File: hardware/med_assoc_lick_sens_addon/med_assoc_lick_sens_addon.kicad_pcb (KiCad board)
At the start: 2 copper layers, 50.8 x 52.1 mm, 15 parts, among them J1 Conn_Coaxial, J2 Conn_01x03_Socket, U1 6N139, U2 L7805

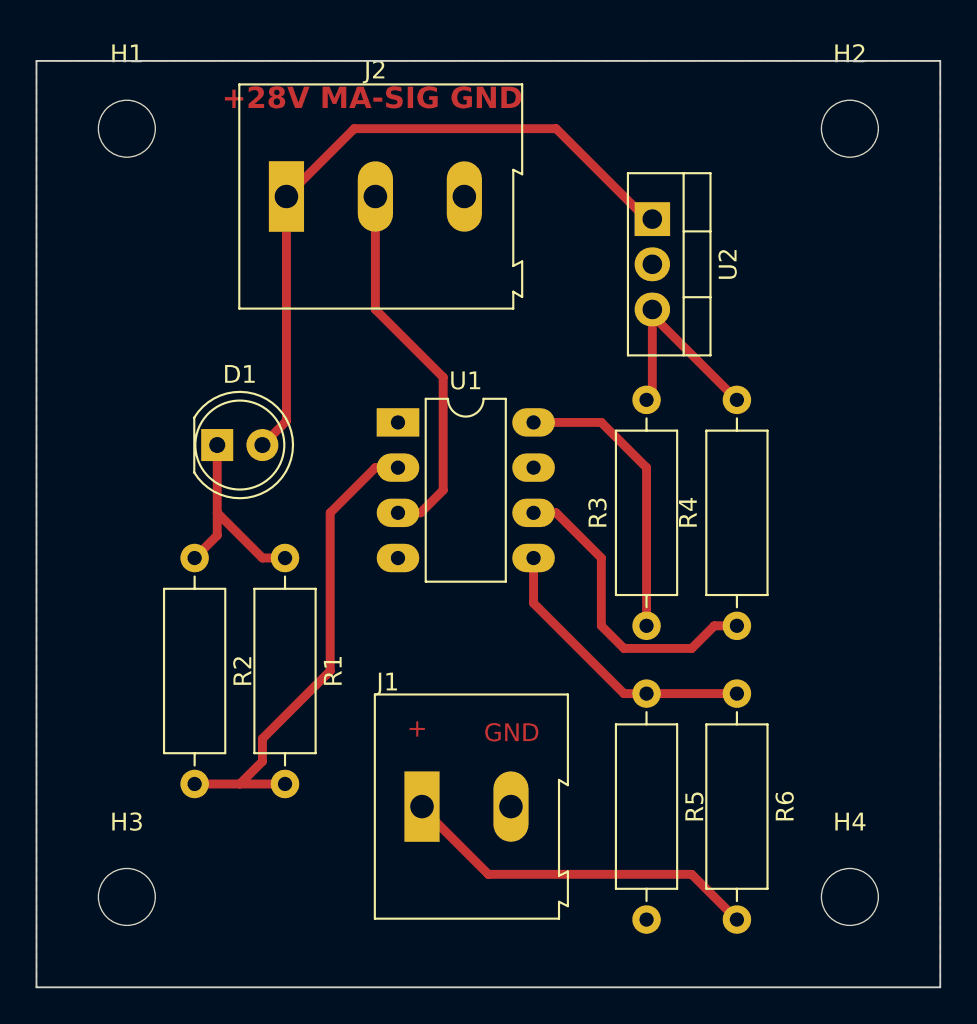
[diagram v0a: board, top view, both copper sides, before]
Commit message: move traces to bottom side of board
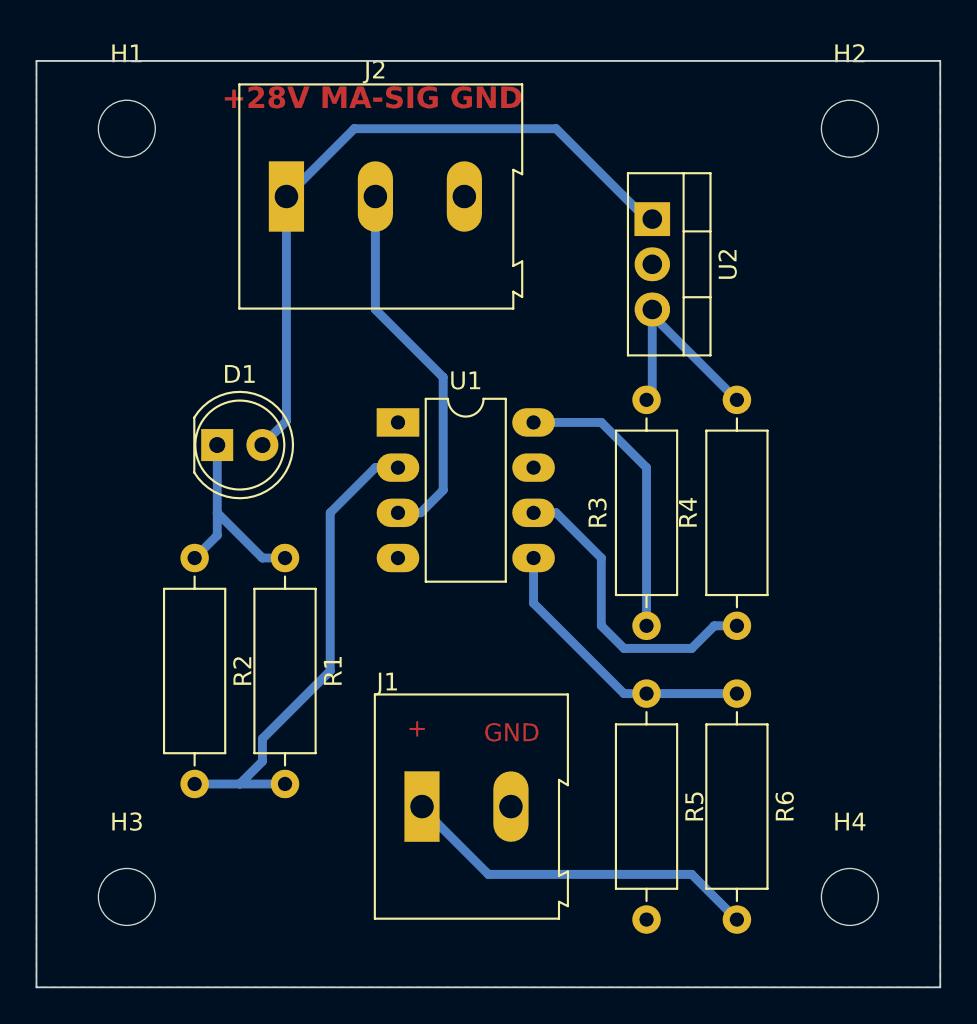
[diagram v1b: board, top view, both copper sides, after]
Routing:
- added copper zone on B.Cu, net GND
- removed copper zone on F.Cu, net GND
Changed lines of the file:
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@@
     (effects (font (size 1 1) (thickness 0.15)) (justify left bottom))
   )
-  (segment (start 152.4 63.5) (end 153.67 63.5) (width 0.5) (layer "F.Cu") (net 1))
-  (segment (start 149.86 60.96) (end 149.86 62.23) (width 0.5) (layer "F.Cu") (net 1))
-  (segment (start 149.86 57.15) (end 149.86 60.96) (width 0.5) (layer "F.Cu") (net 1))
-  (segment (start 149.86 60.96) (end 152.4 63.5) (width 0.5) (layer "F.Cu") (net 1))
-  (segment (start 149.86 62.23) (end 148.59 63.5) (width 0.5) (layer "F.Cu") (net 1))
-  (segment (start 174.315 44.45) (end 173.99 44.45) (width 0.5) (layer "F.Cu") (net 2))
-  (segment (start 153.75 43.18) (end 153.75 55.8) (width 0.5) (layer "F.Cu") (net 2))
-  (segment (start 153.75 55.8) (end 152.4 57.15) (width 0.5) (layer "F.Cu") (net 2))
-  (segment (start 168.91 39.37) (end 157.56 39.37) (width 0.5) (layer "F.Cu") (net 2))
-  (segment (start 157.56 39.37) (end 153.75 43.18) (width 0.5) (layer "F.Cu") (net 2))
-  (segment (start 173.99 44.45) (end 168.91 39.37) (width 0.5) (layer "F.Cu") (net 2))
-  (segment (start 165.1 81.28) (end 161.37 77.55) (width 0.5) (layer "F.Cu") (net 3))
-  (segment (start 161.37 77.55) (end 161.37 77.47) (width 0.5) (layer "F.Cu") (net 3))
-  (segment (start 176.53 81.28) (end 165.1 81.28) (width 0.5) (layer "F.Cu") (net 3))
-  (segment (start 179.07 83.82) (end 176.53 81.28) (width 0.5) (layer "F.Cu") (net 3))
-  (segment (start 158.75 43.18) (end 158.75 49.53) (width 0.5) (layer "F.Cu") (net 5))
-  (segment (start 162.56 59.69) (end 161.29 60.96) (width 0.5) (layer "F.Cu") (net 5))
-  (segment (start 161.29 60.96) (end 160.02 60.96) (width 0.5) (layer "F.Cu") (net 5))
-  (segment (start 158.75 49.53) (end 162.56 53.34) (width 0.5) (layer "F.Cu") (net 5))
-  (segment (start 162.56 53.34) (end 162.56 59.69) (width 0.5) (layer "F.Cu") (net 5))
-  (segment (start 151.13 76.2) (end 152.4 74.93) (width 0.5) (layer "F.Cu") (net 6))
-  (segment (start 156.21 69.85) (end 156.21 60.96) (width 0.5) (layer "F.Cu") (net 6))
-  (segment (start 152.4 74.93) (end 152.4 73.66) (width 0.5) (layer "F.Cu") (net 6))
-  (segment (start 158.75 58.42) (end 160.02 58.42) (width 0.5) (layer "F.Cu") (net 6))
-  (segment (start 151.13 76.2) (end 153.67 76.2) (width 0.5) (layer "F.Cu") (net 6))
-  (segment (start 148.59 76.2) (end 151.13 76.2) (width 0.5) (layer "F.Cu") (net 6))
-  (segment (start 152.4 73.66) (end 156.21 69.85) (width 0.5) (layer "F.Cu") (net 6))
-  (segment (start 156.21 60.96) (end 158.75 58.42) (width 0.5) (layer "F.Cu") (net 6))
-  (segment (start 173.99 58.42) (end 171.45 55.88) (width 0.5) (layer "F.Cu") (net 7))
-  (segment (start 171.45 55.88) (end 167.64 55.88) (width 0.5) (layer "F.Cu") (net 7))
-  (segment (start 173.99 67.31) (end 173.99 58.42) (width 0.5) (layer "F.Cu") (net 7))
-  (segment (start 174.315 49.855) (end 179.07 54.61) (width 0.5) (layer "F.Cu") (net 8))
-  (segment (start 174.315 49.53) (end 174.315 54.285) (width 0.5) (layer "F.Cu") (net 8))
-  (segment (start 174.315 54.285) (end 173.99 54.61) (width 0.5) (layer "F.Cu") (net 8))
-  (segment (start 174.315 49.53) (end 174.315 49.855) (width 0.5) (layer "F.Cu") (net 8))
-  (segment (start 171.45 67.31) (end 171.45 63.5) (width 0.5) (layer "F.Cu") (net 9))
-  (segment (start 179.07 67.31) (end 177.8 67.31) (width 0.5) (layer "F.Cu") (net 9))
-  (segment (start 177.8 67.31) (end 176.53 68.58) (width 0.5) (layer "F.Cu") (net 9))
-  (segment (start 168.91 60.96) (end 167.64 60.96) (width 0.5) (layer "F.Cu") (net 9))
-  (segment (start 172.72 68.58) (end 171.45 67.31) (width 0.5) (layer "F.Cu") (net 9))
-  (segment (start 176.53 68.58) (end 172.72 68.58) (width 0.5) (layer "F.Cu") (net 9))
-  (segment (start 171.45 63.5) (end 168.91 60.96) (width 0.5) (layer "F.Cu") (net 9))
-  (segment (start 172.72 71.12) (end 173.99 71.12) (width 0.5) (layer "F.Cu") (net 10))
-  (segment (start 167.64 63.5) (end 167.64 66.04) (width 0.5) (layer "F.Cu") (net 10))
-  (segment (start 167.64 66.04) (end 172.72 71.12) (width 0.5) (layer "F.Cu") (net 10))
-  (segment (start 179.07 71.12) (end 173.99 71.12) (width 0.5) (layer "F.Cu") (net 10))
-  (zone (net 4) (net_name "GND") (layer "F.Cu") (hatch edge 0.5)
-    (connect_pads (clearance 0.5))
-    (min_thickness 0.25) (filled_areas_thickness no)
-    (fill yes (thermal_gap 0.5) (thermal_bridge_width 0.5))
-    (polygon
-      (pts
-        (xy 139.7 35.56)
-        (xy 190.5 35.56)
-        (xy 190.5 87.63)
-        (xy 139.7 87.63)
-      )
-    )
-  )
+  (segment (start 152.4 63.5) (end 153.67 63.5) (width 0.5) (layer "B.Cu") (net 1))
+  (segment (start 149.86 60.96) (end 149.86 62.23) (width 0.5) (layer "B.Cu") (net 1))
+  (segment (start 149.86 57.15) (end 149.86 60.96) (width 0.5) (layer "B.Cu") (net 1))
+  (segment (start 149.86 60.96) (end 152.4 63.5) (width 0.5) (layer "B.Cu") (net 1))
+  (segment (start 149.86 62.23) (end 148.59 63.5) (width 0.5) (layer "B.Cu") (net 1))
+  (segment (start 174.315 44.45) (end 173.99 44.45) (width 0.5) (layer "B.Cu") (net 2))
+  (segment (start 153.75 43.18) (end 153.75 55.8) (width 0.5) (layer "B.Cu") (net 2))
+  (segment (start 153.75 55.8) (end 152.4 57.15) (width 0.5) (layer "B.Cu") (net 2))
+  (segment (start 168.91 39.37) (end 157.56 39.37) (width 0.5) (layer "B.Cu") (net 2))
+  (segment (start 157.56 39.37) (end 153.75 43.18) (width 0.5) (layer "B.Cu") (net 2))
+  (segment (start 173.99 44.45) (end 168.91 39.37) (width 0.5) (layer "B.Cu") (net 2))
+  (segment (start 165.1 81.28) (end 161.37 77.55) (width 0.5) (layer "B.Cu") (net 3))
+  (segment (start 161.37 77.55) (end 161.37 77.47) (width 0.5) (layer "B.Cu") (net 3))
+  (segment (start 176.53 81.28) (end 165.1 81.28) (width 0.5) (layer "B.Cu") (net 3))
+  (segment (start 179.07 83.82) (end 176.53 81.28) (width 0.5) (layer "B.Cu") (net 3))
+  (segment (start 158.75 43.18) (end 158.75 49.53) (width 0.5) (layer "B.Cu") (net 5))
+  (segment (start 162.56 59.69) (end 161.29 60.96) (width 0.5) (layer "B.Cu") (net 5))
+  (segment (start 161.29 60.96) (end 160.02 60.96) (width 0.5) (layer "B.Cu") (net 5))
+  (segment (start 158.75 49.53) (end 162.56 53.34) (width 0.5) (layer "B.Cu") (net 5))
+  (segment (start 162.56 53.34) (end 162.56 59.69) (width 0.5) (layer "B.Cu") (net 5))
+  (segment (start 151.13 76.2) (end 152.4 74.93) (width 0.5) (layer "B.Cu") (net 6))
+  (segment (start 156.21 69.85) (end 156.21 60.96) (width 0.5) (layer "B.Cu") (net 6))
+  (segment (start 152.4 74.93) (end 152.4 73.66) (width 0.5) (layer "B.Cu") (net 6))
+  (segment (start 158.75 58.42) (end 160.02 58.42) (width 0.5) (layer "B.Cu") (net 6))
+  (segment (start 151.13 76.2) (end 153.67 76.2) (width 0.5) (layer "B.Cu") (net 6))
+  (segment (start 148.59 76.2) (end 151.13 76.2) (width 0.5) (layer "B.Cu") (net 6))
+  (segment (start 152.4 73.66) (end 156.21 69.85) (width 0.5) (layer "B.Cu") (net 6))
+  (segment (start 156.21 60.96) (end 158.75 58.42) (width 0.5) (layer "B.Cu") (net 6))
+  (segment (start 173.99 58.42) (end 171.45 55.88) (width 0.5) (layer "B.Cu") (net 7))
+  (segment (start 171.45 55.88) (end 167.64 55.88) (width 0.5) (layer "B.Cu") (net 7))
+  (segment (start 173.99 67.31) (end 173.99 58.42) (width 0.5) (layer "B.Cu") (net 7))
+  (segment (start 174.315 49.855) (end 179.07 54.61) (width 0.5) (layer "B.Cu") (net 8))
+  (segment (start 174.315 49.53) (end 174.315 54.285) (width 0.5) (layer "B.Cu") (net 8))
+  (segment (start 174.315 54.285) (end 173.99 54.61) (width 0.5) (layer "B.Cu") (net 8))
+  (segment (start 174.315 49.53) (end 174.315 49.855) (width 0.5) (layer "B.Cu") (net 8))
+  (segment (start 171.45 67.31) (end 171.45 63.5) (width 0.5) (layer "B.Cu") (net 9))
+  (segment (start 179.07 67.31) (end 177.8 67.31) (width 0.5) (layer "B.Cu") (net 9))
+  (segment (start 177.8 67.31) (end 176.53 68.58) (width 0.5) (layer "B.Cu") (net 9))
+  (segment (start 168.91 60.96) (end 167.64 60.96) (width 0.5) (layer "B.Cu") (net 9))
+  (segment (start 172.72 68.58) (end 171.45 67.31) (width 0.5) (layer "B.Cu") (net 9))
+  (segment (start 176.53 68.58) (end 172.72 68.58) (width 0.5) (layer "B.Cu") (net 9))
+  (segment (start 171.45 63.5) (end 168.91 60.96) (width 0.5) (layer "B.Cu") (net 9))
+  (segment (start 172.72 71.12) (end 173.99 71.12) (width 0.5) (layer "B.Cu") (net 10))
+  (segment (start 167.64 63.5) (end 167.64 66.04) (width 0.5) (layer "B.Cu") (net 10))
+  (segment (start 167.64 66.04) (end 172.72 71.12) (width 0.5) (layer "B.Cu") (net 10))
+  (segment (start 179.07 71.12) (end 173.99 71.12) (width 0.5) (layer "B.Cu") (net 10))
   (zone (net 0) (net_name "") (layers "F&B.Cu") (hatch edge 0.5)
     (connect_pads (clearance 0))
@@
       )
     )
+  )
+  (zone (net 4) (net_name "GND") (layer "B.Cu") (hatch edge 0.5)
+    (connect_pads (clearance 0.5))
+    (min_thickness 0.25) (filled_areas_thickness no)
+    (fill yes (thermal_gap 0.5) (thermal_bridge_width 0.5))
+    (polygon
+      (pts
+        (xy 139.7 35.56)
+        (xy 190.5 35.56)
+        (xy 190.5 87.63)
+        (xy 139.7 87.63)
+      )
+    )
